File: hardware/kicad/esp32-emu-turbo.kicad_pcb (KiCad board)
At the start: 4 copper layers, 160 x 75 mm, 78 parts, among them J1 USB-C-16P, J3 JST-PH-2P, J4 FPC-40P-0.5mm, SW1 SW-SMD-5.1x5.1, SW10 SW-SMD-5.1x5.1, SW11 SW-SMD-5.1x5.1, SW12 SW-SMD-5.1x5.1, SW13 SW-SMD-5.1x5.1, SW2 SW-SMD-5.1x5.1, SW3 SW-SMD-5.1x5.1, SW4 SW-SMD-5.1x5.1, SW5 SW-SMD-5.1x5.1, SW6 SW-SMD-5.1x5.1, SW7 SW-SMD-5.1x5.1, SW8 SW-SMD-5.1x5.1, SW9 SW-SMD-5.1x5.1, U1 ESP32-S3-WROOM-1-N16R8, U2 ESOP-8, U3 SOT-223, U5 SOP-16, U6 TF-01A

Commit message: fix(bom): add 7 missing PAM8403 passives to BOM + CPL
C21 (100nF VREF bypass), C22 (0.47µF DC-block), C23-C25 (1µF VDD/PVDD
decoupling), R20-R21 (20kΩ INL/INR bias) were on PCB but missing from
JLCPCB manufacturing files. Updated jlcpcb_export.py, all BOM/CPL copies,
bom-summary.md. DFA 9/9 pass, BOM-CPL 71/71 consistent.

Co-Authored-By: Claude Opus 4.6 (1M context) <noreply@anthropic.com>
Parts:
- removed the J3 at (80.0, 57.5)
- removed the L1 at (110.0, 52.5)
- removed the U5 at (30.0, 29.5)
- added C1: C_0805, C_0805, B.Cu at (122.0, 48.5)
- added C2: C_1206, C_1206, B.Cu at (125.0, 62.5)
- added C25: C_0805, C_0805, B.Cu at (31.5, 37.5)
- added FID1: Fiducial, Fiducial, F.Cu at (5.00, 5.00)
- added FID2: Fiducial, Fiducial, F.Cu at (155.0, 5.00)
- added FID3: Fiducial, Fiducial, F.Cu at (5.00, 70.0)
- C18: renamed from R20; value R_0805 -> C_0805; footprint R_0805 -> C_0805
- C19: renamed from R21; value R_0805 -> C_1206; footprint R_0805 -> C_1206
- C20: renamed from C19; value C_1206 -> C_0805; footprint C_1206 -> C_0805
- C24: renamed from C2; value C_1206 -> C_0805; footprint C_1206 -> C_0805
- C3: renamed from R18; value R_0805 -> C_0805; footprint R_0805 -> C_0805
- C4: renamed from R4; value R_0805 -> C_0805; footprint R_0805 -> C_0805
- J3: renamed from R3; value R_0805 -> JST-PH-2P; footprint R_0805 -> JST-PH-2P
- L1: renamed from R2; value R_0805 -> SMD-4x4x2; footprint R_0805 -> SMD-4x4x2
- R1: renamed from C3; value C_0805 -> R_0805; footprint C_0805 -> R_0805
- R15: renamed from C5; value C_0805 -> R_0805; footprint C_0805 -> R_0805
- R16: renamed from C7; value C_0805 -> R_0805; footprint C_0805 -> R_0805
- R19: renamed from C6; value C_0805 -> R_0805; footprint C_0805 -> R_0805
- R2: renamed from C4; value C_0805 -> R_0805; footprint C_0805 -> R_0805
- R20: renamed from C23; value C_0805 -> R_0805; footprint C_0805 -> R_0805
- R21: renamed from C24; value C_0805 -> R_0805; footprint C_0805 -> R_0805
- U5: renamed from R1; value R_0805 -> SOP-16; footprint R_0805 -> SOP-16
- moved C24 103.9 mm to (29.4, 22.0)
- moved C23 86.1 mm to (38.0, 29.5)
- moved C18 84.8 mm to (118.0, 55.0)
- moved C17 78.3 mm to (110.0, 35.0)
- moved C19 76.7 mm to (110.0, 58.5)
- moved R16 62.1 mm to (115.0, 52.5)
- moved U5 57.5 mm to (30.0, 29.5)
- moved R15 55.1 mm to (98.0, 46.0)
- moved R19 55.1 mm to (103.0, 46.0)
- moved C4 49.2 mm to (92.0, 42.0)
- moved R3 46.1 mm to (65.0, 42.0)
- moved C3 44.0 mm to (69.5, 42.0)
- moved R17 29.8 mm to (25.0, 65.0)
- moved R18 28.3 mm to (32.0, 65.0)
- moved L1 27.8 mm to (110.0, 52.5)
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- renumbered C13 to C10, C14 to C11, C15 to C12, C16 to C13, C20 to C14, C17 to C15, C18 to C16, C22 to C17, C25 to C21, C21 to C22, C1 to C23, C8 to C5, C9 to C6, C10 to C7, C11 to C8, C12 to C9, R13 to R10, R14 to R11, R15 to R12, R19 to R13, R16 to R14, R5 to R17, R6 to R18, R17 to R3, R7 to R4, R8 to R5, R9 to R6, R10 to R7, R11 to R8, R12 to R9
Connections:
- C15 pad 1: VBUS -> (no net)
- C15 pad 2: GND -> (no net)
- C16 pad 1: BAT+ -> (no net)
- C16 pad 2: GND -> (no net)
- C17 pad 1: I2S_DOUT -> VBUS
- C17 pad 2: I2S_DOUT -> GND
- C18 pad 1: GND -> BAT+
- C18 pad 2: I2S_DOUT -> GND
- C19 pad 1: GND -> +5V
- C19 pad 2: I2S_DOUT -> GND
- C20 pad 1: +5V -> (no net)
- C20 pad 2: GND -> (no net)
- C21 pad 1: +5V -> GND
- C21 pad 2: GND -> PAM_VREF
- C22 pad 1: GND -> I2S_DOUT
- C22 pad 2: PAM_VREF -> I2S_DOUT
- C24 pad 1: +3V3 -> GND
- C24 pad 2: GND -> +5V
- C3 pad 2: (no net) -> GND
- C4 pad 1: (no net) -> +3V3
- C4 pad 2: (no net) -> GND
- J3 pad 1: (no net) -> BAT+
- J3 pad 2: (no net) -> GND
- L1 pad 1: USB_CC2 -> BAT+
- L1 pad 2: GND -> LX
- R1 pad 1: +3V3 -> USB_CC1
- R14 pad 1: +5V -> (no net)
- R14 pad 2: IP5306_KEY -> (no net)
- R16 pad 1: (no net) -> +5V
- R16 pad 2: (no net) -> IP5306_KEY
- R17 pad 1: (no net) -> +3V3
- R18 pad 1: (no net) -> +3V3
- R2 pad 1: +3V3 -> USB_CC2
- R20 pad 1: +5V -> GND
- R20 pad 2: GND -> I2S_DOUT
- R21 pad 2: +5V -> I2S_DOUT
- R3 pad 1: +3V3 -> (no net)
- U5 pad 1: USB_CC1 -> (no net)
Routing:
- net BAT+: track 116.0 -> 121.0 mm
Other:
- board text added: "BATT"
- board text added: "LCD"

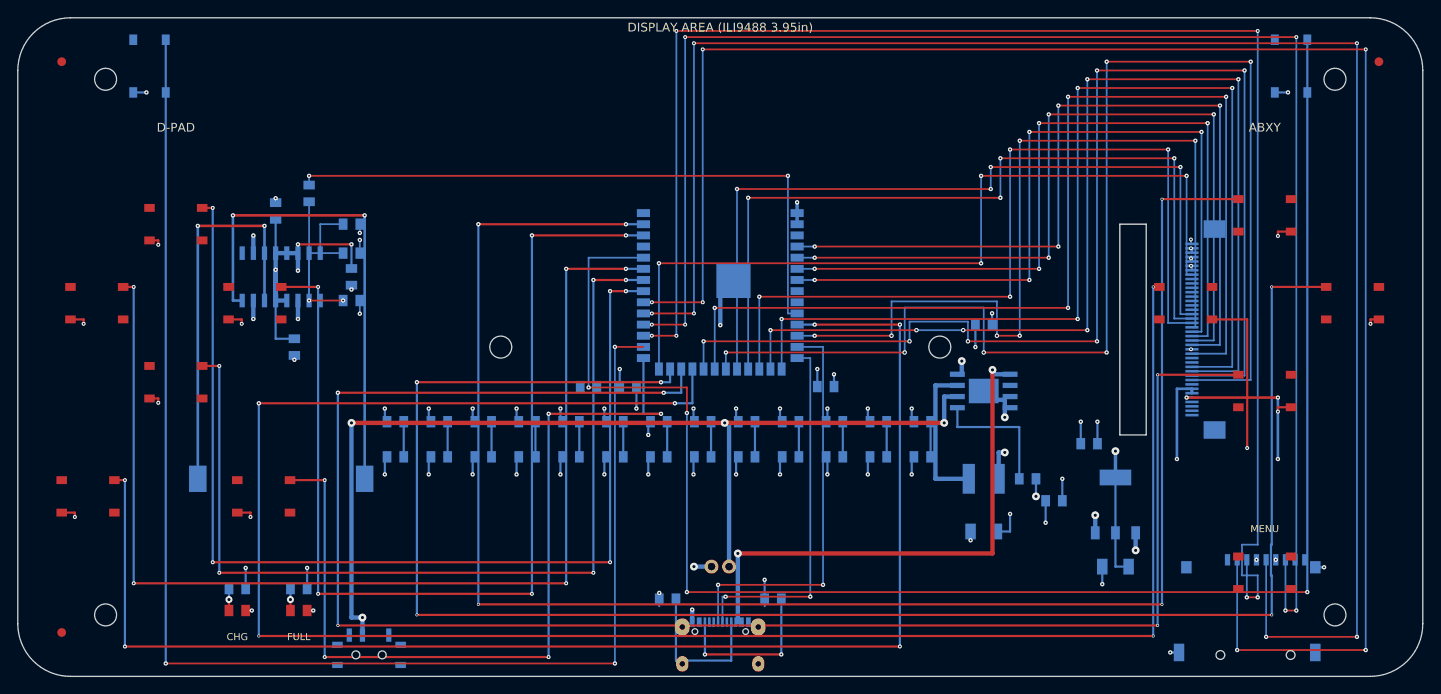
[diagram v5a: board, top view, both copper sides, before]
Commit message: feat(pcb): fix all JLCDFM violations + add 22 factory-rule DFM tests
PCB generator fixes:
- Via annular ring: 0.46/0.20→0.50/0.20mm (AR 0.13→0.15mm)
- Trace spacing: clearance 0.10→0.15mm (JLCPCB standard)
- Add 3 fiducial marks for SMT pick-and-place alignment
- USB-C pad-to-edge: 0.225→0.525mm (move 0.3mm inward)
- USB-C shield mask margin: -0.1→0mm (no negative expansion)
- BTN_B jog W_DATA in U6 pin gap, USB_D- column shift
- ESP32 GND vert width reduced for LCD_RST via clearance
- R20/R21/C21 GND vias shifted for SPK+ clearance
- Silkscreen labels moved away from drill holes
- J3 battery connector moved 5mm closer to J1 USB-C
- Collinear segment overlaps fixed

22 new JLCDFM factory-rule tests on ALL components:
trace spacing, annular ring, pad-to-edge, fiducials,
via clearances, unconnected traces/vias, soldermask,
silkscreen, PTH spacing, sharp corners

Results: 114/114 DFM + 9/9 DFA + 0 collisions

Co-Authored-By: Claude Opus 4.6 (1M context) <noreply@anthropic.com>
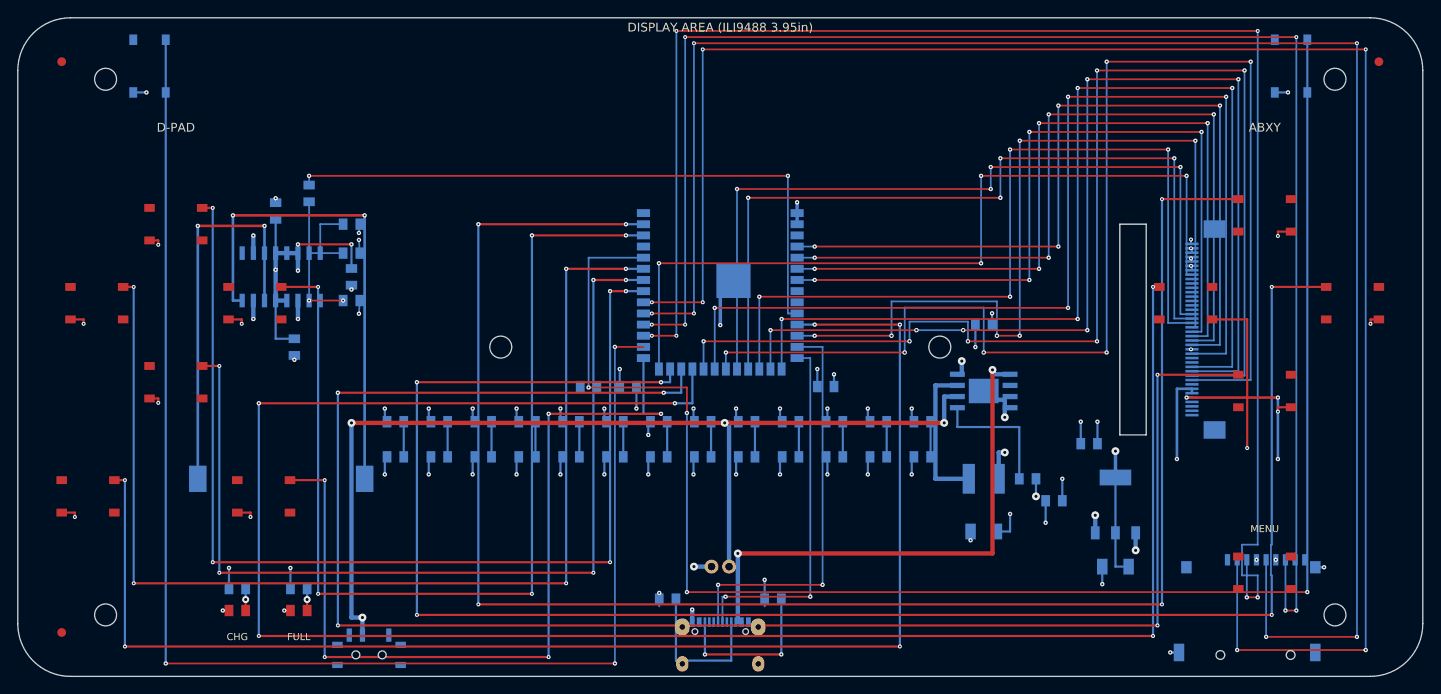
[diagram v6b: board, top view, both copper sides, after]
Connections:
- LED1 pad 1: (no net) -> GND
- LED1 pad 2: GND -> (no net)
- LED2 pad 1: (no net) -> GND
- LED2 pad 2: GND -> (no net)
- R17 pad 1: +3V3 -> (no net)
- R17 pad 2: (no net) -> +3V3
- R18 pad 1: +3V3 -> (no net)
- R18 pad 2: (no net) -> +3V3
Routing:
- net I2S_DOUT: track 96.7 -> 91.3 mm
- net +5V: track 46.9 -> 43.4 mm
- net +3V3: track 59.6 -> 59.1 mm

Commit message: fix(pcb): SD_CS/BTN_R reroute + MH via AR + THT collision detection
Routing fixes:
- SD_CS stagger y=72.0→71.0 (clears U6 NPTH drill, gap 0.97mm)
- BTN_R F.Cu jog y=65.4→64.0 between x=137-146.5 (bypasses SW13 pads)
- MH detour vias 0.51/0.25→0.56/0.25mm (AR 0.13→0.155mm)

Collision detection:
- THT pad registration on both F.Cu/B.Cu layers
- Known pad nets for J1 shield (GND) and J3 (BAT+)

Known remaining JLCDFM issues (need architectural reroute):
- BTN_X/Y F.Cu channels cross J1 shield THT zone y=68-70
- BTN_SELECT crosses SW_PWR NPTH zone y=72
- 61 button vias at AR=0.13mm (meets min, below recommended)

Results: 114/114 DFM + 9/9 DFA

Co-Authored-By: Claude Opus 4.6 (1M context) <noreply@anthropic.com>
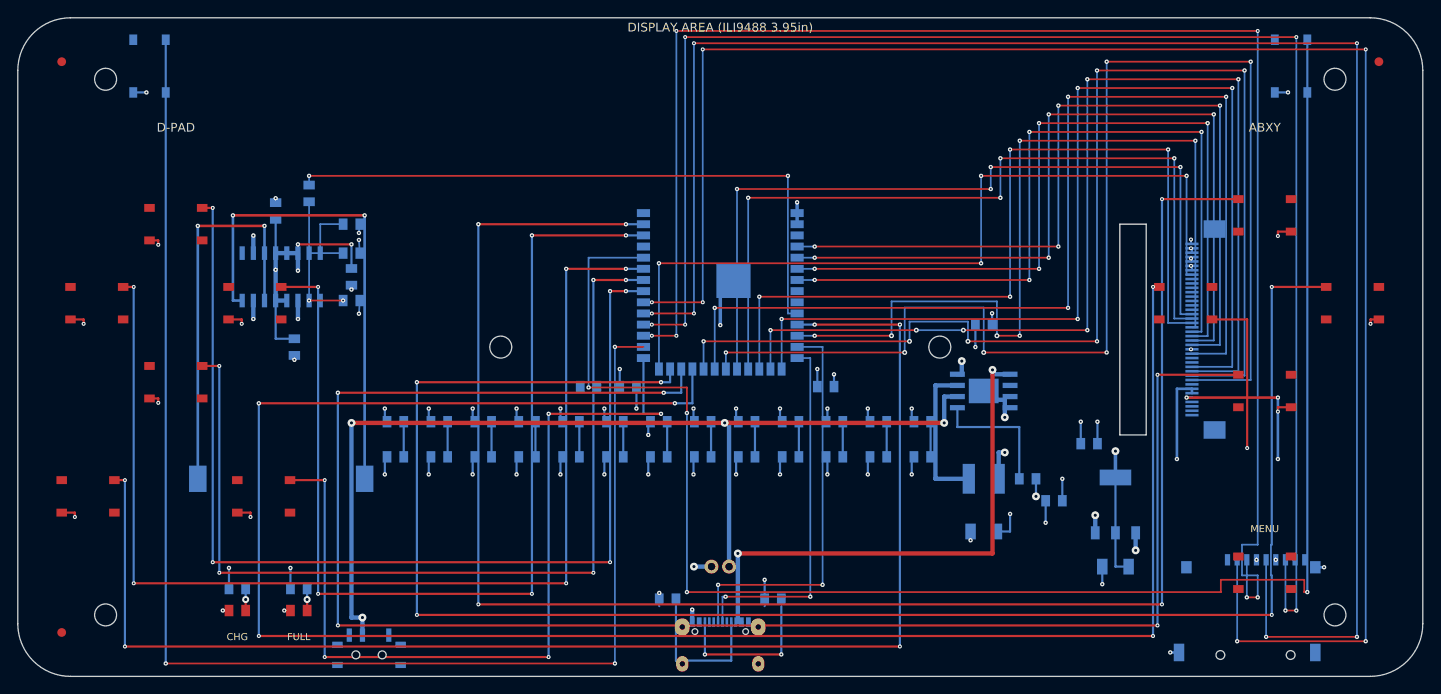
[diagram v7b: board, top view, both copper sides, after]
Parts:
- removed the C2 at (125.0, 62.5)
- removed the FID1 at (5.00, 5.00)
- added FID2: Fiducial, Fiducial, F.Cu at (155.0, 5.00)
- added FID3: Fiducial, Fiducial, F.Cu at (5.00, 70.0)
- C2: renamed from FID2; value Fiducial -> C_1206; footprint Fiducial -> C_1206; moved to B.Cu
- moved FID1 65.0 mm to (5.00, 5.00)
- moved C2 64.9 mm to (125.0, 62.5)
- renumbered FID3 to FID1
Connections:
- C2 pad 1: (no net) -> +3V3
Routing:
- net BTN_R: track 193.1 -> 195.9 mm
- net SD_CS: track 204.4 -> 202.4 mm
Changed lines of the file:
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@@
   (via (at 80.635 38.115) (size 0.5) (drill 0.2) (layers "F.Cu" "B.Cu") (net 14))
   (segment (start 80.635 38.115) (end 101.0 38.115) (width 0.2) (layer "F.Cu") (net 14))
-  (via (at 101.0 38.115) (size 0.51) (drill 0.25) (layers "F.Cu" "B.Cu") (net 14))
+  (via (at 101.0 38.115) (size 0.56) (drill 0.25) (layers "F.Cu" "B.Cu") (net 14))
   (segment (start 101.0 38.115) (end 101.0 33.0) (width 0.2) (layer "B.Cu") (net 14))
   (segment (start 101.0 33.0) (end 110.0 33.0) (width 0.2) (layer "B.Cu") (net 14))
   (segment (start 110.0 33.0) (end 110.0 38.115) (width 0.2) (layer "B.Cu") (net 14))
-  (via (at 110.0 38.115) (size 0.51) (drill 0.25) (layers "F.Cu" "B.Cu") (net 14))
+  (via (at 110.0 38.115) (size 0.56) (drill 0.25) (layers "F.Cu" "B.Cu") (net 14))
   (segment (start 110.0 38.115) (end 124.0 38.115) (width 0.2) (layer "F.Cu") (net 14))
   (via (at 124.0 38.115) (size 0.5) (drill 0.2) (layers "F.Cu" "B.Cu") (net 14))
@@
   (via (at 78.095 36.845) (size 0.5) (drill 0.2) (layers "F.Cu" "B.Cu") (net 16))
   (segment (start 78.095 36.845) (end 101.55 36.845) (width 0.2) (layer "F.Cu") (net 16))
-  (via (at 101.55 36.845) (size 0.51) (drill 0.25) (layers "F.Cu" "B.Cu") (net 16))
+  (via (at 101.55 36.845) (size 0.56) (drill 0.25) (layers "F.Cu" "B.Cu") (net 16))
   (segment (start 101.55 36.845) (end 101.55 34.6) (width 0.2) (layer "B.Cu") (net 16))
   (segment (start 101.55 34.6) (end 108.2 34.6) (width 0.2) (layer "B.Cu") (net 16))
   (segment (start 108.2 34.6) (end 108.2 36.845) (width 0.2) (layer "B.Cu") (net 16))
-  (via (at 108.2 36.845) (size 0.51) (drill 0.25) (layers "F.Cu" "B.Cu") (net 16))
+  (via (at 108.2 36.845) (size 0.56) (drill 0.25) (layers "F.Cu" "B.Cu") (net 16))
   (segment (start 108.2 36.845) (end 122.9 36.845) (width 0.2) (layer "F.Cu") (net 16))
   (via (at 122.9 36.845) (size 0.5) (drill 0.2) (layers "F.Cu" "B.Cu") (net 16))
@@
   (segment (start 85.715 40.0) (end 85.715 35.575) (width 0.2) (layer "B.Cu") (net 17))
   (via (at 85.715 35.575) (size 0.5) (drill 0.2) (layers "F.Cu" "B.Cu") (net 17))
-  (segment (start 85.715 35.575) (end 102.34 35.575) (width 0.2) (layer "F.Cu") (net 17))
-  (via (at 102.34 35.575) (size 0.51) (drill 0.25) (layers "F.Cu" "B.Cu") (net 17))
-  (segment (start 102.34 35.575) (end 107.66 35.575) (width 0.2) (layer "B.Cu") (net 17))
-  (via (at 107.66 35.575) (size 0.51) (drill 0.25) (layers "F.Cu" "B.Cu") (net 17))
-  (segment (start 107.66 35.575) (end 121.8 35.575) (width 0.2) (layer "F.Cu") (net 17))
+  (segment (start 85.715 35.575) (end 102.32 35.575) (width 0.2) (layer "F.Cu") (net 17))
+  (via (at 102.32 35.575) (size 0.56) (drill 0.25) (layers "F.Cu" "B.Cu") (net 17))
+  (segment (start 102.32 35.575) (end 107.68 35.575) (width 0.2) (layer "B.Cu") (net 17))
+  (via (at 107.68 35.575) (size 0.56) (drill 0.25) (layers "F.Cu" "B.Cu") (net 17))
+  (segment (start 107.68 35.575) (end 121.8 35.575) (width 0.2) (layer "F.Cu") (net 17))
   (via (at 121.8 35.575) (size 0.5) (drill 0.2) (layers "F.Cu" "B.Cu") (net 17))
   (segment (start 121.8 35.575) (end 121.8 7.0) (width 0.2) (layer "B.Cu") (net 17))
@@
   (via (at 90.75 36.21) (size 0.5) (drill 0.2) (layers "F.Cu" "B.Cu") (net 10))
   (segment (start 90.75 36.21) (end 99.5 36.21) (width 0.2) (layer "F.Cu") (net 10))
-  (via (at 99.5 36.21) (size 0.51) (drill 0.25) (layers "F.Cu" "B.Cu") (net 10))
+  (via (at 99.5 36.21) (size 0.56) (drill 0.25) (layers "F.Cu" "B.Cu") (net 10))
   (segment (start 99.5 36.21) (end 99.5 32.3) (width 0.2) (layer "B.Cu") (net 10))
   (segment (start 99.5 32.3) (end 111.5 32.3) (width 0.2) (layer "B.Cu") (net 10))
   (segment (start 111.5 32.3) (end 111.5 36.21) (width 0.2) (layer "B.Cu") (net 10))
-  (via (at 111.5 36.21) (size 0.51) (drill 0.25) (layers "F.Cu" "B.Cu") (net 10))
+  (via (at 111.5 36.21) (size 0.56) (drill 0.25) (layers "F.Cu" "B.Cu") (net 10))
   (segment (start 111.5 36.21) (end 114.1 36.21) (width 0.2) (layer "F.Cu") (net 10))
   (via (at 114.1 36.21) (size 0.5) (drill 0.2) (layers "F.Cu" "B.Cu") (net 10))
@@
   (segment (start 78.0 3.5999999999999996) (end 153.5 3.5999999999999996) (width 0.2) (layer "F.Cu") (net 23))
   (via (at 153.5 3.5999999999999996) (size 0.46) (drill 0.2) (layers "F.Cu" "B.Cu") (net 23))
-  (segment (start 153.5 3.5999999999999996) (end 153.5 72.0) (width 0.2) (layer "B.Cu") (net 23))
-  (via (at 153.5 72.0) (size 0.5) (drill 0.2) (layers "F.Cu" "B.Cu") (net 23))
-  (segment (start 153.5 72.0) (end 138.86 72.0) (width 0.2) (layer "F.Cu") (net 23))
-  (via (at 138.86 72.0) (size 0.5) (drill 0.2) (layers "F.Cu" "B.Cu") (net 23))
-  (segment (start 138.86 72.0) (end 138.86 61.724000000000004) (width 0.2) (layer "B.Cu") (net 23))
+  (segment (start 153.5 3.5999999999999996) (end 153.5 71.0) (width 0.2) (layer "B.Cu") (net 23))
+  (via (at 153.5 71.0) (size 0.5) (drill 0.2) (layers "F.Cu" "B.Cu") (net 23))
+  (segment (start 153.5 71.0) (end 138.86 71.0) (width 0.2) (layer "F.Cu") (net 23))
+  (via (at 138.86 71.0) (size 0.5) (drill 0.2) (layers "F.Cu" "B.Cu") (net 23))
+  (segment (start 138.86 71.0) (end 138.86 61.724000000000004) (width 0.2) (layer "B.Cu") (net 23))
   (segment (start 88.75 33.67) (end 87.7 33.67) (width 0.2) (layer "B.Cu") (net 26))
   (segment (start 87.7 33.67) (end 87.7 18.0) (width 0.2) (layer "B.Cu") (net 26))
@@
   (segment (start 146.85 2.5) (end 146.85 65.4) (width 0.25) (layer "B.Cu") (net 38))
   (via (at 146.85 65.4) (size 0.5) (drill 0.2) (layers "F.Cu" "B.Cu") (net 38))
-  (segment (start 146.85 65.4) (end 76.2 65.4) (width 0.2) (layer "F.Cu") (net 38))
+  (segment (start 146.85 65.4) (end 146.5 65.4) (width 0.2) (layer "F.Cu") (net 38))
+  (segment (start 146.5 65.4) (end 146.5 64.0) (width 0.2) (layer "F.Cu") (net 38))
+  (segment (start 146.5 64.0) (end 137.0 64.0) (width 0.2) (layer "F.Cu") (net 38))
+  (segment (start 137.0 64.0) (end 137.0 65.4) (width 0.2) (layer "F.Cu") (net 38))
+  (segment (start 137.0 65.4) (end 76.2 65.4) (width 0.2) (layer "F.Cu") (net 38))
   (via (at 76.2 65.4) (size 0.5) (drill 0.2) (layers "F.Cu" "B.Cu") (net 38))
   (segment (start 76.2 65.4) (end 76.2 45.0) (width 0.2) (layer "B.Cu") (net 38))
